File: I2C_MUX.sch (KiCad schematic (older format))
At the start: 25 parts, among them U5 TCA9548ARGER

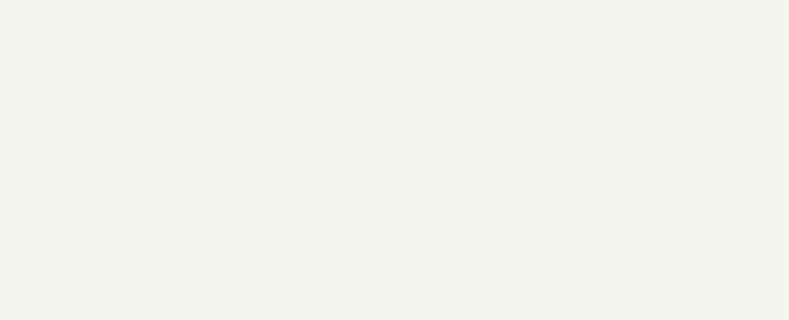
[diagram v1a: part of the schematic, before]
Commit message: SW2 placement changed, BOM cleared, FPGA boot, less ERC errors and wornings
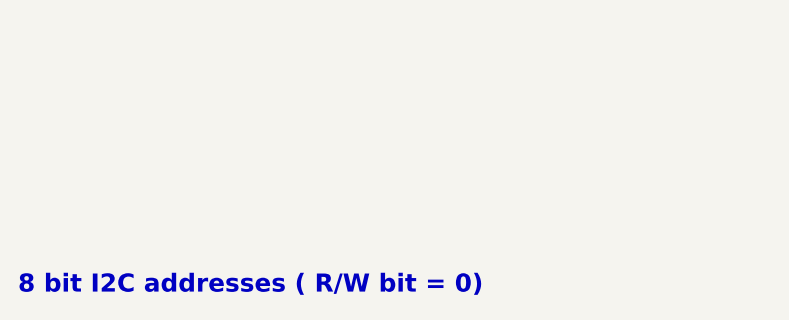
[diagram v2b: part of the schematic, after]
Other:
- note added: "8 bit I2C addresses ( R/W bit = 0)"

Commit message: BOM updated, 25MHz clock level fixed
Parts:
- U5: symbol AMC_FMC_Carrier-PcbDoc-rescue:TCA9548ARGER-Interface_Expansion -> AMC_FMC_Carrier-PcbDoc-rescue:TCA9548ARGER-Interface_Expansion-AMC_FMC_Carrier-PcbDoc-rescue
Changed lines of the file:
@@
 $EndDescr
 $Comp
-L AMC_FMC_Carrier-PcbDoc-rescue:TCA9548ARGER-Interface_Expansion U5
+L AMC_FMC_Carrier-PcbDoc-rescue:TCA9548ARGER-Interface_Expansion-AMC_FMC_Carrier-PcbDoc-rescue U5
 U 1 1 5C5DB690
 P 5150 2900

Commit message: more designators are visible
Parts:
- R274: config (none) -> dnf
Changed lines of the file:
@@
 F 40 "Resistors SMD" H 4650 -870 60  0001 L CNN "Library Name"
 F 41 "This work is licensed under the Creative Commons CC-BY-SA 4.0 License. To the extent that circuit schematics that use Licensed Material can be considered to be ‘Adapted Material’, then the copyright holder waives article 3.b of the license with respect to these schematics." H 4650 -960 60  0001 L CNN "License"
+F 42 "dnf" H 4650 2850 50  0001 C CNN "config"
 	1    4650 2850
 	0    1    1    0

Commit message: BOM configuration file edited, updated Marble picture, some components part number changed
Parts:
- U5: Manufacturer Part Number (none) -> TCA9548ARGER; PN TCA9548ARGER -> (none)
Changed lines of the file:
@@
 F 2 "ICs And Semiconductors SMD:QFN50P400X400X100-25N-S220" H 5150 1900 50  0001 C CNN
 F 3 "http://www.ti.com/lit/ds/symlink/tca9548a.pdf" H 5200 3150 50  0001 C CNN
-F 4 "TCA9548ARGER" H 5150 2900 50  0001 C CNN "PN"
+F 4 "TCA9548ARGER" H 5150 2900 50  0001 C CNN "Manufacturer Part Number"
 	1    5150 2900
 	1    0    0    -1

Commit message: Rename library AMC_FMC_Carrier-PcbDoc-rescue as marble_misc
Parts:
- U5: symbol AMC_FMC_Carrier-PcbDoc-rescue:TCA9548ARGER-Interface_Expansion-AMC_FMC_Carrier-PcbDoc-rescue -> marble_misc:TCA9548ARGER-Interface_Expansion-AMC_FMC_Carrier-PcbDoc-rescue
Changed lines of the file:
@@
 $EndDescr
 $Comp
-L AMC_FMC_Carrier-PcbDoc-rescue:TCA9548ARGER-Interface_Expansion-AMC_FMC_Carrier-PcbDoc-rescue U5
+L marble_misc:TCA9548ARGER-Interface_Expansion-AMC_FMC_Carrier-PcbDoc-rescue U5
 U 1 1 5C5DB690
 P 5150 2900

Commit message: Strip extraneous AMC_FMC_Carrier-PcbDoc-rescue and powerMG from symbol names
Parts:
- U5: symbol marble_misc:TCA9548ARGER-Interface_Expansion-AMC_FMC_Carrier-PcbDoc-rescue -> marble_misc:TCA9548ARGER-Interface_Expansion
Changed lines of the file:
@@
 $EndDescr
 $Comp
-L marble_misc:TCA9548ARGER-Interface_Expansion-AMC_FMC_Carrier-PcbDoc-rescue U5
+L marble_misc:TCA9548ARGER-Interface_Expansion U5
 U 1 1 5C5DB690
 P 5150 2900
